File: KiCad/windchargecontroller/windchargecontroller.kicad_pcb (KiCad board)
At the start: 2 copper layers, 50 parts, among them J1 1935789, J2 ESW-110-12-T-D, J3 1935789, J4 1935789, Q1 Si7336ADP, Q10 2N5087, Q11 Si7336ADP, Q12 Si7336ADP, Q2 Si7336ADP, Q3 Si7336ADP, Q4 2N5210, Q5 2N5087, Q6 Si7336ADP, Q7 2N5210, Q8 2N5087, Q9 2N5210

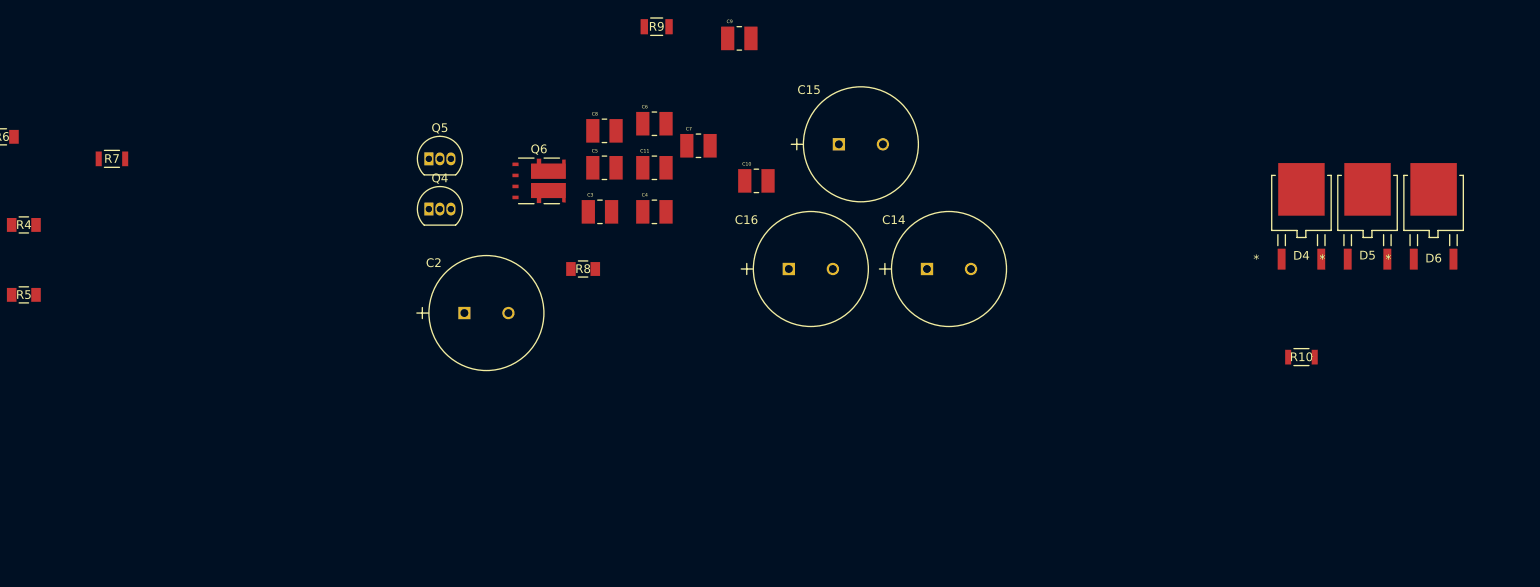
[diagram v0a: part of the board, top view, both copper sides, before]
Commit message: Worked on schematic and pcb
added inductor, moved stuff around on pcb into general area to get a rough idea for size. Getting schematic checked for problems but almost done
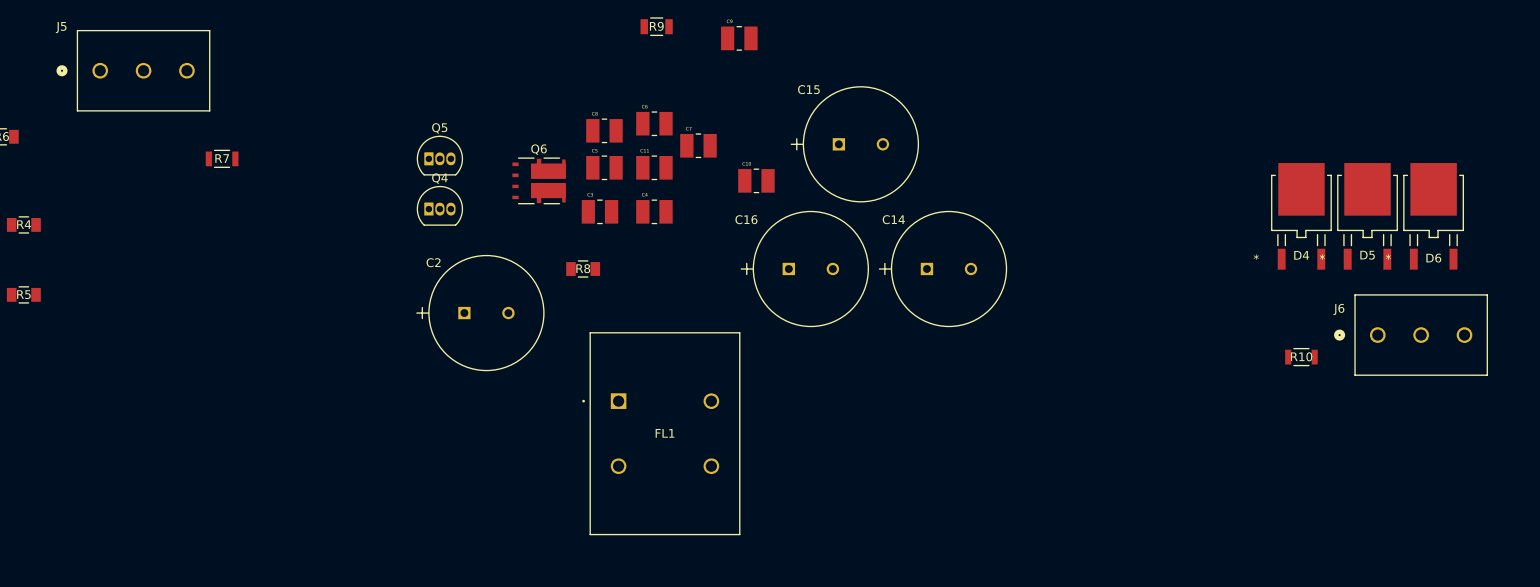
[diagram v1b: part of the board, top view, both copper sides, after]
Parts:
- added FL1: 7448031002, footprints:LIND_1-4_2-3_WE-CMBNC_TYPE-M_WRE, F.Cu at (134.6, 81.3)
- added J5: 1935789, footprints:CONN_1935789_PXC, F.Cu at (74.8, 43.2)
- added J6: 1935789, footprints:CONN_1935789_PXC, F.Cu at (222.2, 73.7)
- moved R7 12.7 mm to (88.9, 53.3)
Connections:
- net Isolator2 renamed Shunt2
- net Isolator3 renamed Shunt3
- net Isolator5 renamed Shunt5
- net Isolator7 renamed Shunt7
- net Net-(C10-Pad2) renamed /L2-
- net Net-(C4-Pad1) renamed /L1-
- net Power1Out renamed Shunt6
- net Power2Out renamed Shunt8
- D1 pad 2: Isolator1 -> Net-(D1-Pad2)
- D2 pad 2: Isolator1 -> Net-(D1-Pad2)
- D3 pad 2: Isolator1 -> Net-(D1-Pad2)
- D5 pad 1: Isolator4 -> Net-(D5-Pad1)
- D5 pad 3: Isolator4 -> Net-(D5-Pad1)
- D6 pad 1: Isolator4 -> Net-(D5-Pad1)
- D6 pad 3: Isolator4 -> Net-(D5-Pad1)
- J2 pad 02: Isolator1 -> Shunt1
- J2 pad 10: Isolator4 -> Shunt4
- R10 pad 2: Isolator4 -> Shunt4
- R7 pad 1: Isolator1 -> Shunt1

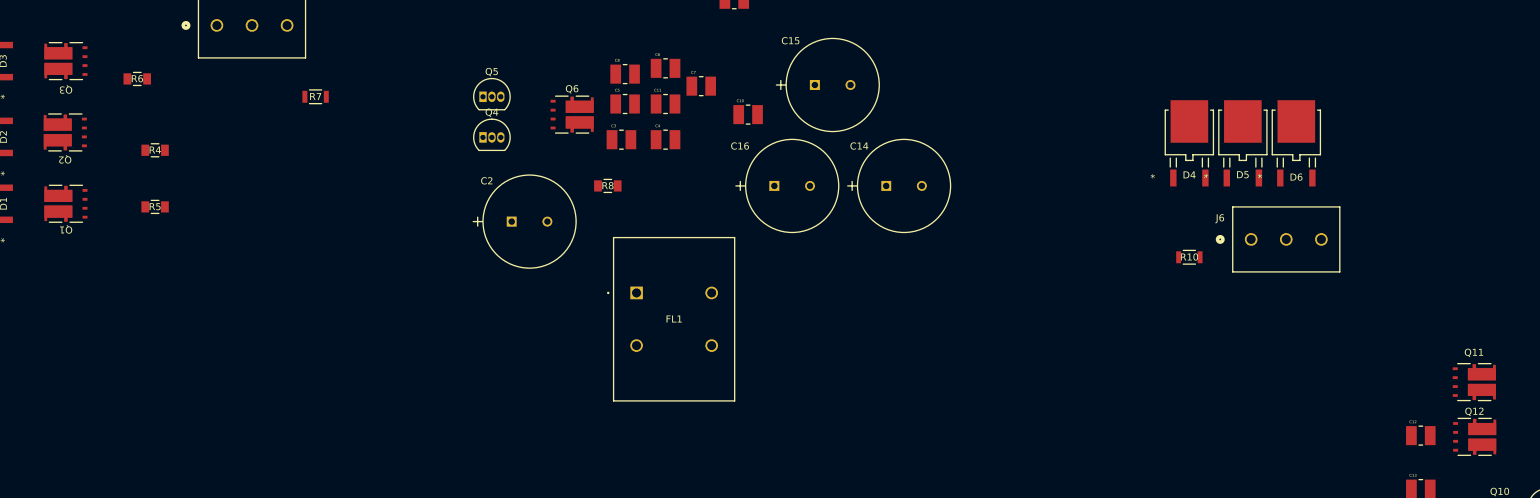
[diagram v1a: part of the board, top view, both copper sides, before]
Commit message: updated kicad and commented ltspice
fixed an incorrect wiring situation in kicad schematic and started process of labelling ltspice schematics
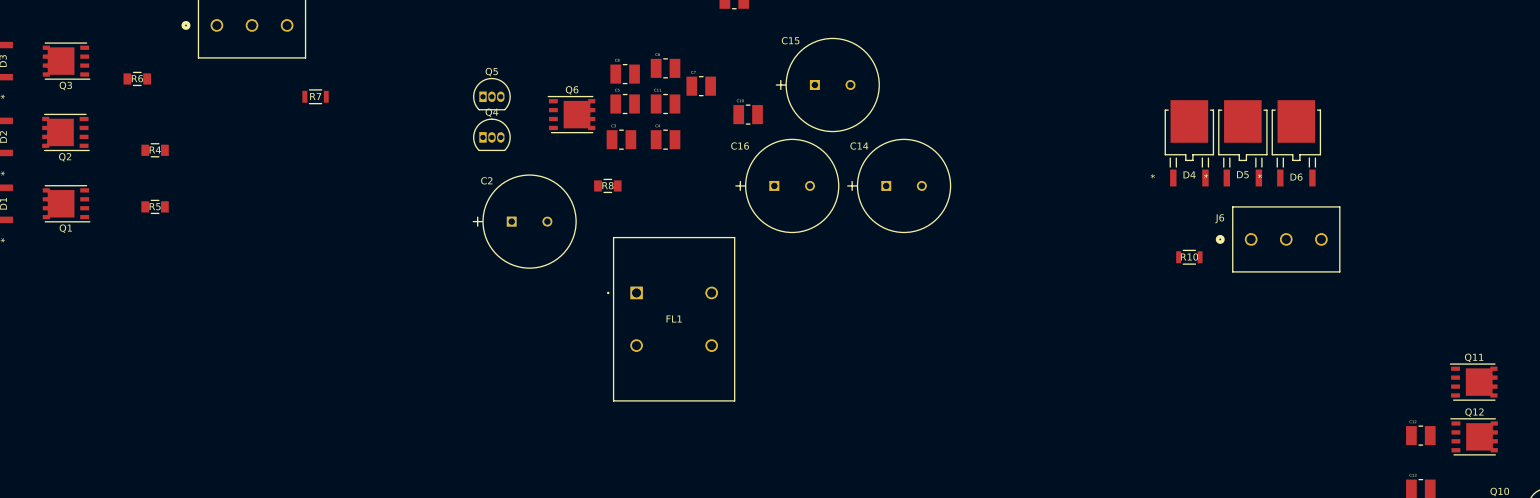
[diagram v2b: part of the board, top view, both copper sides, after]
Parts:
- Q1, Q11, Q12, Q2, Q3, Q6: footprint footprints:SQJ500AEP-T1_GE3_VIS -> Package_SO:PowerPAK_SO-8_Single
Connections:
- net Shunt6 renamed Power1Out
- net Shunt8 renamed Power2Out
- FL1 pad 1: Vdrive -> Shunt2

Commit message: WCC V1.0
placed components and made first version of PCB
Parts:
- added G***: LOGO, footprints:bonfire, F.Cu at (140.5, 67.2)
- J2: value ESW-110-12-T-D -> ESQ-120-XX-X-D-XX; footprint footprints:SAMTEC_ESW-110-12-T-D -> footprints:SAMTEC_ESQ-120-XX-X-D-XX
- moved J4 179.8 mm to (219.2, 50.2), turned to -90 degrees
- moved J3 143.4 mm to (219.2, 82.7), turned to -90 degrees
- moved C1 96.5 mm to (115.2, 89.7)
- moved R2 95.8 mm to (95.9, 76.5)
- moved J2 93.7 mm to (138.2, 94.7), turned to 180 degrees
- moved R3 89.5 mm to (83.1, 75.7), turned to 90 degrees
- moved J1 87.2 mm to (80.1, 96.6)
- moved Q8 77.9 mm to (199.4, 75.3), turned to -90 degrees
- moved R1 73.0 mm to (94.4, 96.8), turned to 90 degrees
- moved Q4 72.8 mm to (182.7, 79.0), turned to -90 degrees
- moved R12 71.8 mm to (210.8, 62.7), turned to 90 degrees
- moved R11 67.4 mm to (194.9, 76.5), turned to -90 degrees
- moved Q7 67.2 mm to (205.9, 75.3), turned to -90 degrees
- moved Q5 67.0 mm to (174.6, 79.0), turned to -90 degrees
- moved Q11 65.0 mm to (195.7, 65.1), turned to 90 degrees
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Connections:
- net /L1- renamed /FL1_con
- net /L2- renamed /D4_con
- net Net-(C6-Pad2) renamed /R9_con
- net Net-(D1-Pad2) renamed /DC+
- net Net-(D5-Pad1) renamed /Loadswitch
- net Net-(D5-Pad2) renamed /Q11_con
- net Net-(D6-Pad2) renamed /Q12_con
- net Net-(Q1-Pad4) renamed /R4_con
- net Net-(Q10-Pad1) renamed /Q12_drive
- net Net-(Q11-Pad4) renamed /Q11_drive
- net Net-(Q2-Pad4) renamed /R5_con
- net Net-(Q3-Pad4) renamed /R6_con
- net Net-(Q4-Pad1) renamed /Q6_drive
- D1 pad 1: Phase_A -> PhaseA+
- D1 pad 3: Phase_A -> PhaseA+
- D2 pad 1: Phase_B -> PhaseB+
- D2 pad 3: Phase_B -> PhaseB+
- D3 pad 1: Phase_C -> PhaseC+
- D3 pad 3: Phase_C -> PhaseC+
- J1 pad 1: Net-(J1-Pad1) -> PhaseA-
- J1 pad 2: Net-(J1-Pad2) -> PhaseB-
- J1 pad 3: Net-(J1-Pad3) -> PhaseC-
- J2 pad 01: Vdrive -> GND
- J2 pad 02: Shunt1 -> GND
- J2 pad 03: Brake_sig -> Vdrive
- J2 pad 04: Shunt2 -> PhaseC-
- J2 pad 05: Net-(J1-Pad3) -> Brake_sig
- J2 pad 06: PWM_sig -> PhaseB-
- J2 pad 07: Net-(J1-Pad2) -> PhaseA+
- J2 pad 08: Shunt3 -> PhaseA-
- J2 pad 09: Net-(J1-Pad1) -> PhaseC+
- J2 pad 10: Shunt4 -> unconnected-(J2-Pad10)
- J2 pad 11: Phase_A -> PhaseB+
- J2 pad 12: PowerSW1 -> unconnected-(J2-Pad12)
- J2 pad 13: Phase_B -> Shunt1
- J2 pad 14: Shunt5 -> unconnected-(J2-Pad14)
- J2 pad 15: Phase_C -> Shunt2
- J2 pad 16: Power1Out -> unconnected-(J2-Pad16)
- J2 pad 17: Shunt7 -> unconnected-(J2-Pad17)
- J2 pad 18: PowerSW2 -> unconnected-(J2-Pad18)
- J2 pad 19: Power2Out -> unconnected-(J2-Pad19)
- J2 pad 20: GND -> unconnected-(J2-Pad20)
- J5 pad 2: unconnected-(J5-Pad2) -> GND
- J6 pad 2: unconnected-(J6-Pad2) -> GND
- Q1 pad 5: Phase_A -> PhaseA+
- Q2 pad 5: Phase_B -> PhaseB+
- Q3 pad 5: Phase_C -> PhaseC+
- R1 pad 1: Net-(J1-Pad1) -> PhaseA-
- R1 pad 2: Phase_A -> PhaseA+
- R2 pad 1: Net-(J1-Pad2) -> PhaseB-
- R2 pad 2: Phase_B -> PhaseB+
- R3 pad 1: Net-(J1-Pad3) -> PhaseC-
- R3 pad 2: Phase_C -> PhaseC+
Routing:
- net Power2Out: track 0.00 -> 128.9 mm
- net GND: track 0.00 -> 124.8 mm, vias 0 -> 8
- net Shunt7: track 0.00 -> 118.9 mm
- net /DC+: track 0.00 -> 108.8 mm
- net Shunt3: track 0.00 -> 97.9 mm
- net Shunt4: track 0.00 -> 89.9 mm
- net PowerSW2: track 0.00 -> 87.2 mm
- net Power1Out: track 0.00 -> 78.5 mm
- net Shunt2: track 0.00 -> 77.2 mm
- net PowerSW1: track 0.00 -> 70.4 mm
- net Vdrive: track 0.00 -> 66.4 mm
- net Shunt1: track 0.00 -> 60.5 mm
- net Shunt5: track 0.00 -> 59.6 mm
- net PWM_sig: track 0.00 -> 50.7 mm
- net /Q12_drive: track 0.00 -> 49.3 mm
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- added copper zone on F.Cu, net /DC+
- added copper zone on F.Cu, net /FL1_con
- added copper zone on B.Cu, net GND
- added copper zone on F.Cu, net GND
- added copper zone on F.Cu, net Net-(C10-Pad1)
- added copper zone on F.Cu, net Net-(C11-Pad1)
- added copper zone on F.Cu, net PhaseA+
- added copper zone on F.Cu, net PhaseA-
- added copper zone on F.Cu, net PhaseB+
- added copper zone on F.Cu, net PhaseB-
- added copper zone on F.Cu, net PhaseC+
- added copper zone on F.Cu, net PhaseC-
- added copper zone on F.Cu, net Shunt1
- added copper zone on F.Cu, net Shunt3
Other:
- board outline added: 151.9 x 68.6 mm
- board text added: "Don't give up, skeleton!"
- board text added: "GND"
- board text added: "P1Out"
- board text added: "P2Out"
- board text added: "PWM"
- board text added: "P_SW1"
- board text added: "P_SW2"
- board text added: "PhaseA"
- board text added: "PhaseA-"
- board text added: "PhaseB"
- board text added: "PhaseB-"
- board text added: "PhaseC"
- board text added: "PhaseC-"
- board text added: "Shunt1"
- board text added: "Shunt2"
- board text added: "Shunt3"
- board text added: "Shunt4"
- board text added: "Shunt5"
- board text added: "Shunt7"
- board text added: "Vdrive"
- board text added: "WCC V.1.0 K.Q"
- board text added: "brake"

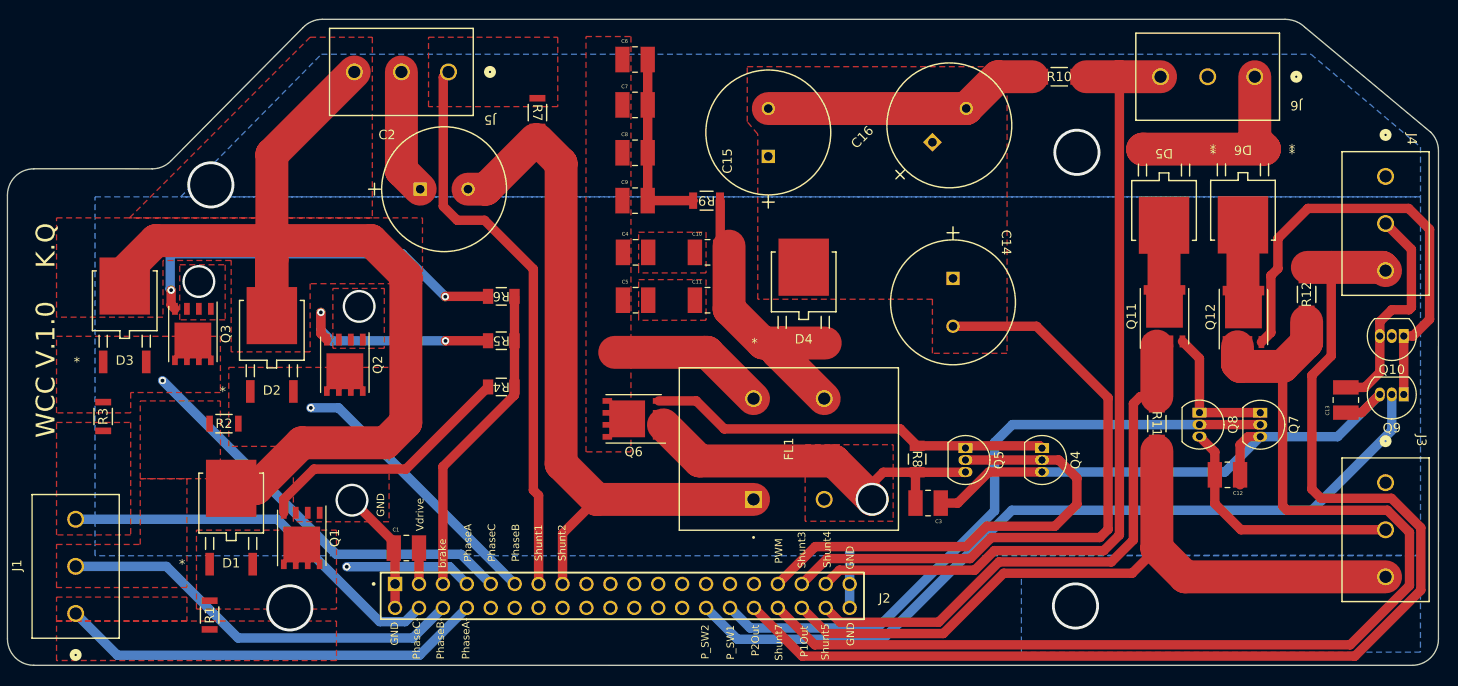
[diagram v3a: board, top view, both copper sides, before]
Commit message: updated WCC Schematic and made  measurement board
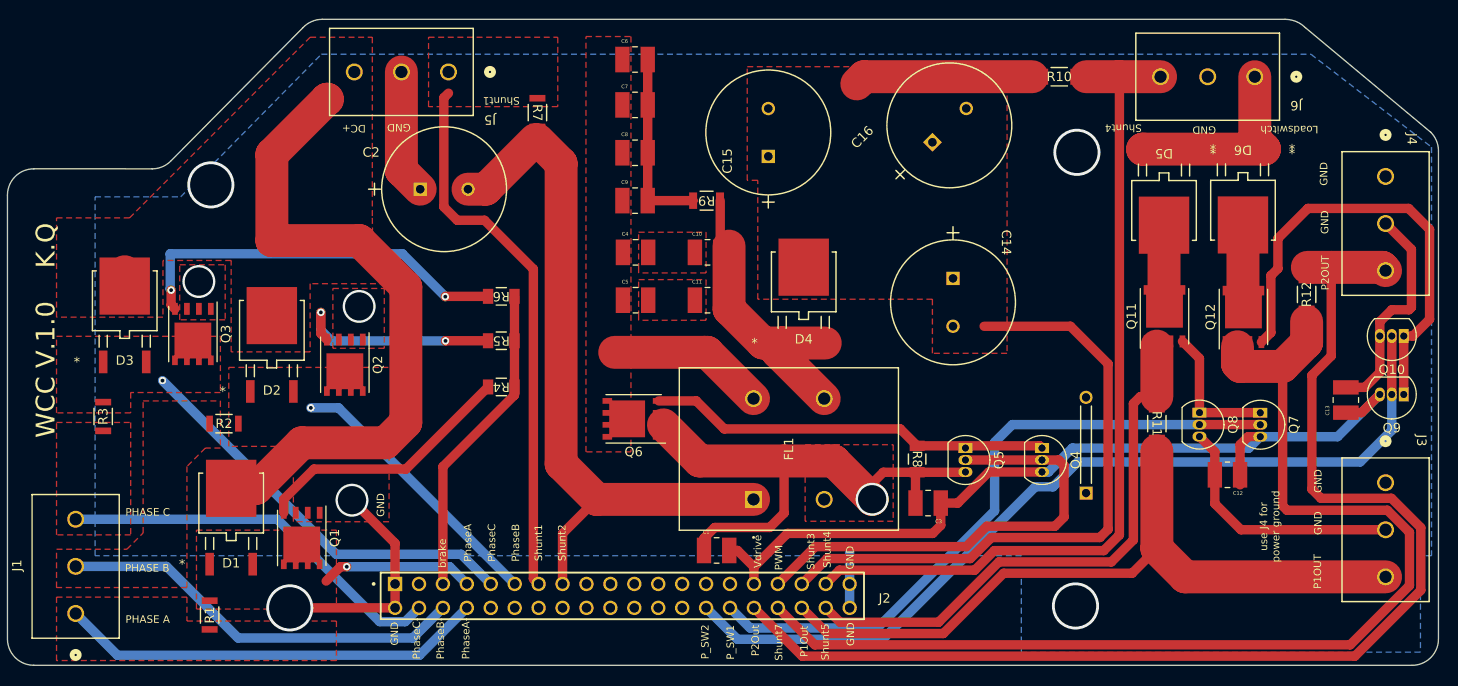
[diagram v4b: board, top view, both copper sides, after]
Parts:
- added REF**: STA_JW60_STP, footprints:STA_JW60_STP, F.Cu at (187.4, 83.8)
- moved C1 32.9 mm to (148.2, 89.9)
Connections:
- J2 pad 03: Vdrive -> unconnected-(J2-Pad03)
- J2 pad 31: unconnected-(J2-Pad31) -> Vdrive
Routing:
- net /DC+: track 108.8 -> 71.1 mm
- net GND: track 124.8 -> 152.8 mm
- net Vdrive: track 66.4 -> 91.7 mm
- net Shunt3: track 97.9 -> 86.2 mm
- net PowerSW2: track 87.2 -> 93.4 mm
- net PhaseA+: track 13.5 -> 16.3 mm
- net Shunt1: track 60.5 -> 58.2 mm
- net PWM_sig: track 50.7 -> 49.5 mm
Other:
- board text added: "DC+"
- board text added: "Loadswitch"
- board text added: "P1OUT"
- board text added: "P2OUT"
- board text added: "PHASE A"
- board text added: "PHASE B"
- board text added: "PHASE C"
- board text added: "use J4 for power ground"
